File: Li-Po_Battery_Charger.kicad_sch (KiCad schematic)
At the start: 0 parts

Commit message: Add title to the Schematic
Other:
- title: (none) -> Li-Po Battery Charger
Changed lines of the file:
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@@
 	(generator_version "10.0")
 	(paper "A4")
+	(title_block
+		(title "Li-Po Battery Charger")
+	)
 	(sheet_instances
 		(path "/"

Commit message: Add USB-C Input
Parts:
- added C1: C_Polarized, Package_SO:SOIC-8_3.9x4.9mm_P1.27mm, symbol Device:C_Polarized
- added C2: C, symbol Device:C
- added D1: ESD9B5.0ST5G, Diode_SMD:D_SOD-923, symbol Diode:ESD9B5.0ST5G
- added F1: Fuse, Package_LCC:PLCC-84_29.3x29.3mm_P1.27mm, symbol Device:Fuse
- added J1: USB_C_Receptacle_PowerOnly_6P, Package_DFN_QFN:WDFN-10-1EP_3x3mm_P0.5mm_EP1.8x2.5mm, symbol Connector:USB_C_Receptacle_PowerOnly_6P
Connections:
- new net: C1.1, C2.1, D1.2 (A2), F1.2
- new net GND: C1.2, C2.2, D1.1 (A1), J1.A12 (GND), J1.B12 (GND), J1.SH (SHIELD)
- new net VBUS: F1.1, J1.A9 (VBUS), J1.B9 (VBUS)
- no-connect marks 0 -> 2

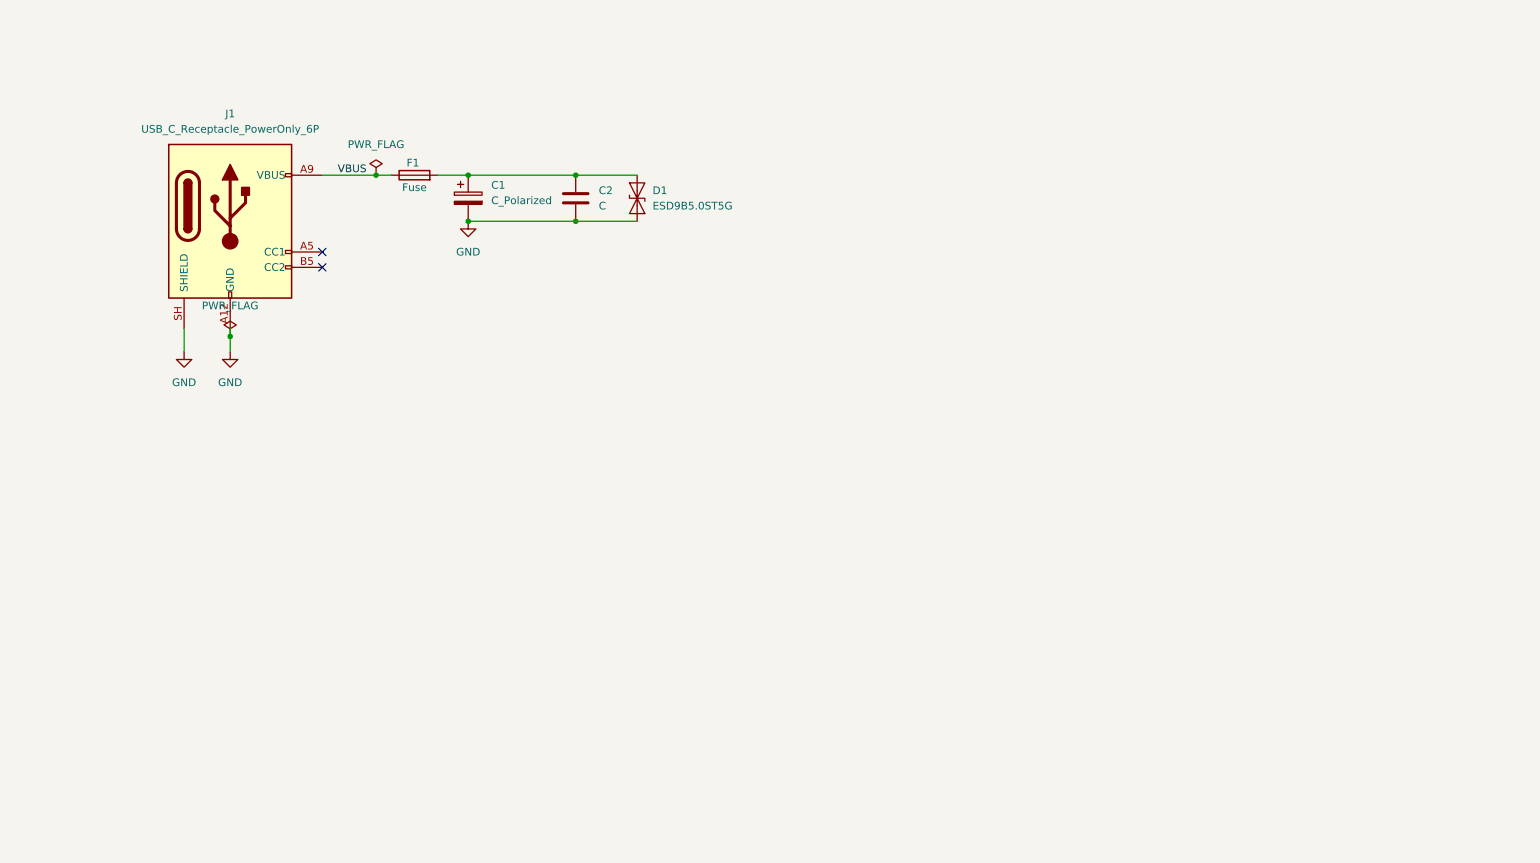
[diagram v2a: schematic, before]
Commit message: Add Battery Charger and Buck Converter
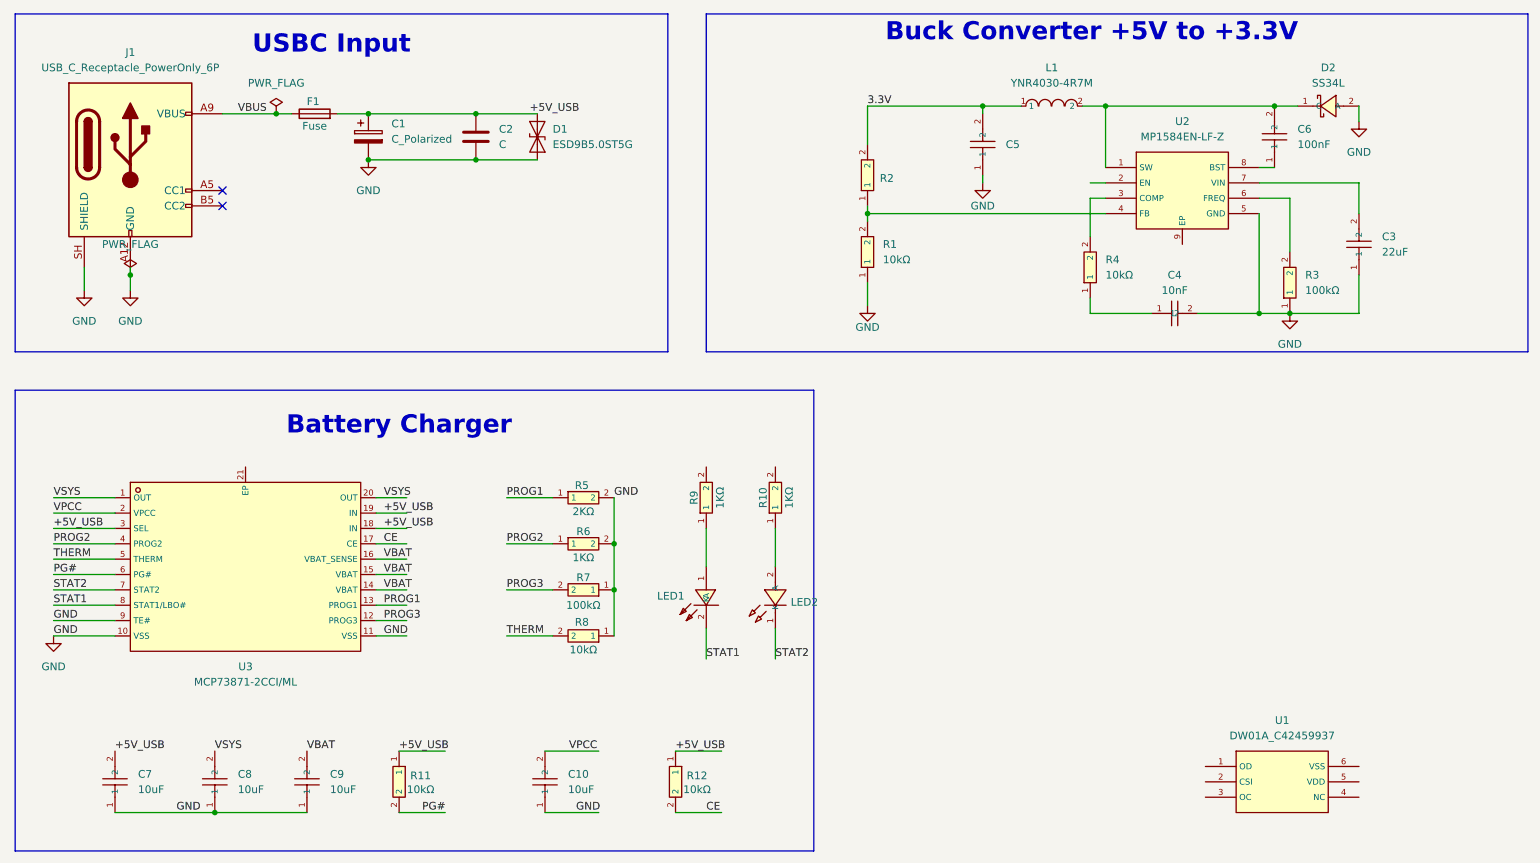
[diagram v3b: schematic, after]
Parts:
- added C10: 10uF, lcsc_footprints:C22392391_C0603, symbol lcsc_imported:TCC0603X5R106M350CT
- added C3: 22uF, lcsc_footprints:C22367828_C0603, symbol lcsc_imported:HGC0603R5226M160NTHJ
- added C4: 10nF, lcsc_footprints:C15195_C0402, symbol lcsc_imported:10nF_(103)_±10%_50V
- added C5: HGC0603R5226M160NTHJ, lcsc_footprints:C22367828_C0603, symbol lcsc_imported:HGC0603R5226M160NTHJ
- added C6: 100nF, lcsc_footprints:C5137616_C0603, symbol lcsc_imported:FCC0603B104K101CT
- added C7, C8, C9: 10uF, lcsc_footprints:C3039641_C0603, symbol lcsc_imported:GCM188D70J106ME36D
- added D2: SS34L, lcsc_footprints:C3003093_SMF_L2_8-W1_8-LS3_7-RD, symbol lcsc_imported:SS34L
- added L1: YNR4030-4R7M, lcsc_footprints:C340391_IND-SMD_L4_0-W4_0, symbol lcsc_imported:YNR4030-4R7M
- added LED1: 0603, lcsc_footprints:C2286_LED-SMD_L1_6-W0_8-R-RD, symbol lcsc_imported:0603
- added LED2: PSC-1608U52GC-G4, lcsc_footprints:C22371297_LED0603-RD_GREEN, symbol lcsc_imported:PSC-1608U52GC-G4
- added R1, R11, R12, R4, R8: 10kΩ, lcsc_footprints:C326912_R0402, symbol lcsc_imported:RT0402DRE0710KL
- added R10, R6, R9: 1KΩ, lcsc_footprints:C11702_R0402, symbol lcsc_imported:1KΩ_(1001)_±1%
- added R2: RMC040231.6K1%N, lcsc_footprints:C325374_R0402, symbol lcsc_imported:RMC040231_6K1%N
- added R3, R7: 100kΩ, lcsc_footprints:C60491_R0402, symbol lcsc_imported:RC0402FR-07100KL
- added R5: 2KΩ, lcsc_footprints:C4109_R0402, symbol lcsc_imported:2KΩ_(2001)_±1%
- added U1: DW01A_C42459937, lcsc_footprints:C42459937_SOT-23-6_L2_9-W1_6-P0_95-LS2_8-BL, symbol lcsc_imported:DW01A_C42459937
- added U2: MP1584EN-LF-Z, lcsc_footprints:C15051_SOIC-8_L5_0-W4_0-P1_27-LS6_0-BL-EP2_0, symbol lcsc_imported:MP1584EN-LF-Z
- added U3: MCP73871-2CCI/ML, lcsc_footprints:C5121473_QFN-20_L4_0-W4_0-P0_50-BL-EP2_7, symbol lcsc_imported:MCP73871-2CCI/ML
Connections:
- net GND: now also C10.1, C3.1, C4.2, C5.1, C7.1, C8.1, C9.1, D2.2 (A), R1.1, R3.1, R5.2, R6.2, R7.1, R8.1, U2.5 (GND), U3.10 (VSS), U3.11 (VSS), U3.9 (TE#)
- net +5V_USB: now reaches C1.1, C2.1, D1.2 (A2), F1.2
- net +5V_USB: now also C7.2, R11.1, R12.1, U3.18 (IN), U3.19 (IN), U3.3 (SEL)
- new net: C6.2, D2.1 (C), L1.2, U2.1 (SW)
- new net: R4.2, U2.3 (COMP)
- new net: R1.2, R2.1, U2.4 (FB)
- new net: R3.2, U2.6 (FREQ)
- new net: C3.2, U2.7 (VIN)
- new net: C6.1, U2.8 (BST)
- new net: LED2.2 (A), R10.1
- new net: C4.1, R4.1
- new net: LED1.1 (A), R9.1
- new net 3.3V: C5.2, L1.1, R2.2
- new net CE: R12.2, U3.17 (CE)
- new net PG#: R11.2, U3.6 (PG#)
- new net PROG1: R5.1, U3.13 (PROG1)
- new net PROG2: R6.1, U3.4 (PROG2)
- new net PROG3: R7.2, U3.12 (PROG3)
- new net STAT1: LED1.2 (K), U3.8 (STAT1/LBO#)
- new net STAT2: LED2.1 (K), U3.7 (STAT2)
- new net THERM: R8.2, U3.5 (THERM)
- new net VBAT: C9.2, U3.14 (VBAT), U3.15 (VBAT), U3.16 (VBAT_SENSE)
- new net VPCC: C10.2, U3.2 (VPCC)
- new net VSYS: C8.2, U3.1 (OUT), U3.20 (OUT)
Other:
- note added: "Battery Charger"
- note added: "Buck Converter +5V to +3.3V"
- note added: "USBC Input"
- moved on the sheet: C1, C2, D1, F1, J1

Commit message: Initial PCB Layout
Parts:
- removed C1: C_Polarized, Package_SO:SOIC-8_3.9x4.9mm_P1.27mm, symbol Device:C_Polarized
- removed C2: C, symbol Device:C
- removed D1: ESD9B5.0ST5G, Diode_SMD:D_SOD-923, symbol Diode:ESD9B5.0ST5G
- removed F1: Fuse, Package_LCC:PLCC-84_29.3x29.3mm_P1.27mm, symbol Device:Fuse
- removed J1: USB_C_Receptacle_PowerOnly_6P, Package_DFN_QFN:WDFN-10-1EP_3x3mm_P0.5mm_EP1.8x2.5mm, symbol Connector:USB_C_Receptacle_PowerOnly_6P
- added BAT1: S2B-PH-K-S(LF)(SN), lcsc_footprints:C173752_CONN-TH_S2B-PH-K-S-LF-SN, symbol lcsc_imported:S2B-PH-K-S(LF)(SN)
- added C1: 10uF, lcsc_footprints:C3039641_C0603, symbol lcsc_imported:GCM188D70J106ME36D
- added C11: 100nF, lcsc_footprints:C5137616_C0603, symbol lcsc_imported:FCC0603B104K101CT
- added C2: 100nF, lcsc_footprints:C5448791_C0402, symbol lcsc_imported:TCC0402X7R104K500AT
- added D1: ESD9B5V, lcsc_footprints:C2905646_SOD-923_L0_8-W0_6-LS1_0-BI-1, symbol lcsc_imported:ESD9B5V
- added F1: 0.50A 24V, lcsc_footprints:C70076_F1206, symbol lcsc_imported:0_50A_24V
- added Q1: FS8205A_C908265, lcsc_footprints:C908265_SOT-23-6_L2_9-W1_6-P0_95-LS2_8-BR, symbol lcsc_imported:FS8205A_C908265
- added USB1: TYPE-C 16P(073), lcsc_footprints:C668624_USB-C-SMD_TYPE-C16PIN_C668624, symbol lcsc_imported:TYPE-C_16P(073)
- C5: value HGC0603R5226M160NTHJ -> 22uF
- R3, R7: value 100kΩ -> 100KΩ
- U1: value DW01A_C42459937 -> DW01A
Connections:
- net +5V_USB: now also R10.2, R9.2, C1.2, C2.2, D1.1 (C), F1.2
- net GND: now also C3.2, R7.2, U2.9 (EP), U3.21 (EP), C1.1, C2.1, D1.2 (A), Q1.3 (S2), USB1.1 (SHELL), USB1.2 (SHELL), USB1.3 (SHELL), USB1.4 (SHELL), USB1.A1B12 (GND), USB1.B1A12 (GND); no longer C3.1, R7.1
- net PROG3: now also R7.1; no longer R7.2
- net VBAT: now also U1.5 (VDD), BAT1.2, C11.1
- net VBUS: now also F1.1, USB1.A4B9 (VBUS), USB1.B4A9 (VBUS)
- net VSYS: now also U2.2 (EN)
- net at U2.7 (VIN): now also C3.1; no longer C3.2
- net OD: now reaches U1.1 (OD)
- net OD: now also Q1.4 (G2)
- net CSI: now reaches U1.2 (CSI)
- net CSI: now also Q1.2 (D1/D2), Q1.5 (D1/D2)
- net OC: now reaches U1.3 (OC)
- net OC: now also Q1.6 (G1)
- net B-: now reaches U1.6 (VSS)
- net B-: now also BAT1.1, C11.2, Q1.1 (S1)
- no-connect marks 2 -> 9
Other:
- note added: "Battery Protection"
- moved on the sheet: R8, U1

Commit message: Final Production Version
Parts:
- removed C10: 10uF, lcsc_footprints:C22392391_C0603, symbol lcsc_imported:TCC0603X5R106M350CT
- removed C3, C5: 22uF, lcsc_footprints:C22367828_C0603, symbol lcsc_imported:HGC0603R5226M160NTHJ
- removed C4: 10nF, lcsc_footprints:C15195_C0402, symbol lcsc_imported:10nF_(103)_±10%_50V
- removed C6: 100nF, lcsc_footprints:C5137616_C0603, symbol lcsc_imported:FCC0603B104K101CT
- removed D2: SS34L, lcsc_footprints:C3003093_SMF_L2_8-W1_8-LS3_7-RD, symbol lcsc_imported:SS34L
- removed F1: 0.50A 24V, lcsc_footprints:C70076_F1206, symbol lcsc_imported:0_50A_24V
- removed L1: YNR4030-4R7M, lcsc_footprints:C340391_IND-SMD_L4_0-W4_0, symbol lcsc_imported:YNR4030-4R7M
- removed R1, R4: 10kΩ, lcsc_footprints:C326912_R0402, symbol lcsc_imported:RT0402DRE0710KL
- removed R2: RMC040231.6K1%N, lcsc_footprints:C325374_R0402, symbol lcsc_imported:RMC040231_6K1%N
- removed R3, R7: 100KΩ, lcsc_footprints:C60491_R0402, symbol lcsc_imported:RC0402FR-07100KL
- removed R6: 1KΩ, lcsc_footprints:C11702_R0402, symbol lcsc_imported:1KΩ_(1001)_±1%
- removed U2: MP1584EN-LF-Z, lcsc_footprints:C15051_SOIC-8_L5_0-W4_0-P1_27-LS6_0-BL-EP2_0, symbol lcsc_imported:MP1584EN-LF-Z
- added C3: 10uF, lcsc_footprints:C3039641_C0603, symbol lcsc_imported:GCM188D70J106ME36D
- added C4: 22uF, lcsc_footprints:C22367828_C0603, symbol lcsc_imported:HGC0603R5226M160NTHJ
- added F1: 1.5A, lcsc_footprints:C118413_F1206, symbol lcsc_imported:1206L150THWR
- added L1: 0.47 µH, lcsc_footprints:C285747_IND-SMD_L4_0-W4_0_CHILISIN_MHCI04012N, symbol lcsc_imported:MHCI04012N-R47M-R8
- added Load1: S2B-PH-K-S(LF)(SN), lcsc_footprints:C173752_CONN-TH_S2B-PH-K-S-LF-SN, symbol lcsc_imported:S2B-PH-K-S(LF)(SN)
- added R1, R2: 5.1KΩ, lcsc_footprints:C25905_R0402, symbol lcsc_imported:5_1KΩ_(5101)_±1%
- added R11: 1KΩ, lcsc_footprints:C11702_R0402, symbol lcsc_imported:1KΩ_(1001)_±1%
- added R12: 10kΩ, lcsc_footprints:C326912_R0402, symbol lcsc_imported:RT0402DRE0710KL
- added R3: 511kΩ, lcsc_footprints:C861454_R0603, symbol lcsc_imported:RT0603BRD07511KL
- added R4: 91 kΩ, lcsc_footprints:C2907077_R0603, symbol lcsc_imported:FRC0603F9102TS
- added R8: 20 kΩ, lcsc_footprints:C93942_R0402, symbol lcsc_imported:RC0402FR-0720KL
- added R9: 100Ω, lcsc_footprints:C106232_R0402, symbol lcsc_imported:RC0402FR-07100RL
- added U1: TPS63802DLAR, lcsc_footprints:C2845237_VSON-10_L3_0-W2_0-P0_50-TL, symbol lcsc_imported:TPS63802DLAR
- renumbered BAT1 to Battery1, C11 to C5, C7 to C6, C8 to C7, C9 to C8, R8 to R10, R11 to R13, R12 to R14, R9 to R6, R10 to R7, U3 to U2, U1 to U3, USB1 to USB-C1
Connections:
- net VPCC is gone; now on net +5V_USB: U2.2 (VPCC)
- net +5V_USB: now also F1.2, R12.1
- net 3.3V: now also C4.2, Load1.2, R3.2, U1.6 (VOUT)
- net CSI: now also R11.2; no longer Q1.2 (D1/D2), Q1.5 (D1/D2)
- net GND: now also C3.1, C4.1, Load1.1, R1.1, R11.1, R2.1, R4.1, R8.2, U1.2 (MODE), U1.3 (AGND), U1.8 (GND)
- net OC: now also Q1.4 (G2); no longer Q1.6 (G1)
- net OD: now also Q1.6 (G1); no longer Q1.4 (G2)
- net PROG2: now also R12.2
- net PROG3: now also R8.1
- net VBAT: now also R9.2; no longer C5.1, U3.5 (VDD)
- net VBUS: now also F1.1
- net VSYS: now also C3.2, U1.1 (EN), U1.10 (VIN)
- net CC1: now reaches USB-C1.A5 (CC1)
- net CC1: now also R1.2
- net CC2: now reaches USB-C1.B5 (CC2)
- net CC2: now also R2.2
- new net: R3.1, R4.2, U1.4 (FB)
- new net: C5.1, R9.1, U3.5 (VDD)
- new net: L1.1, U1.7 (L2)
- new net: L1.2, U1.9 (L1)
- no-connect marks 9 -> 10
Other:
- note added: "Buck-Boost Converter"
- note removed: "Buck Converter +5V to +3.3V"
- moved on the sheet: Battery1, C5, Q1, R13, U3
